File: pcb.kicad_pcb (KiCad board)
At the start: 2 copper layers, 76 parts, among them SW1 SW_Push, U1 ATmega32U4-AU, Y1 16MHz

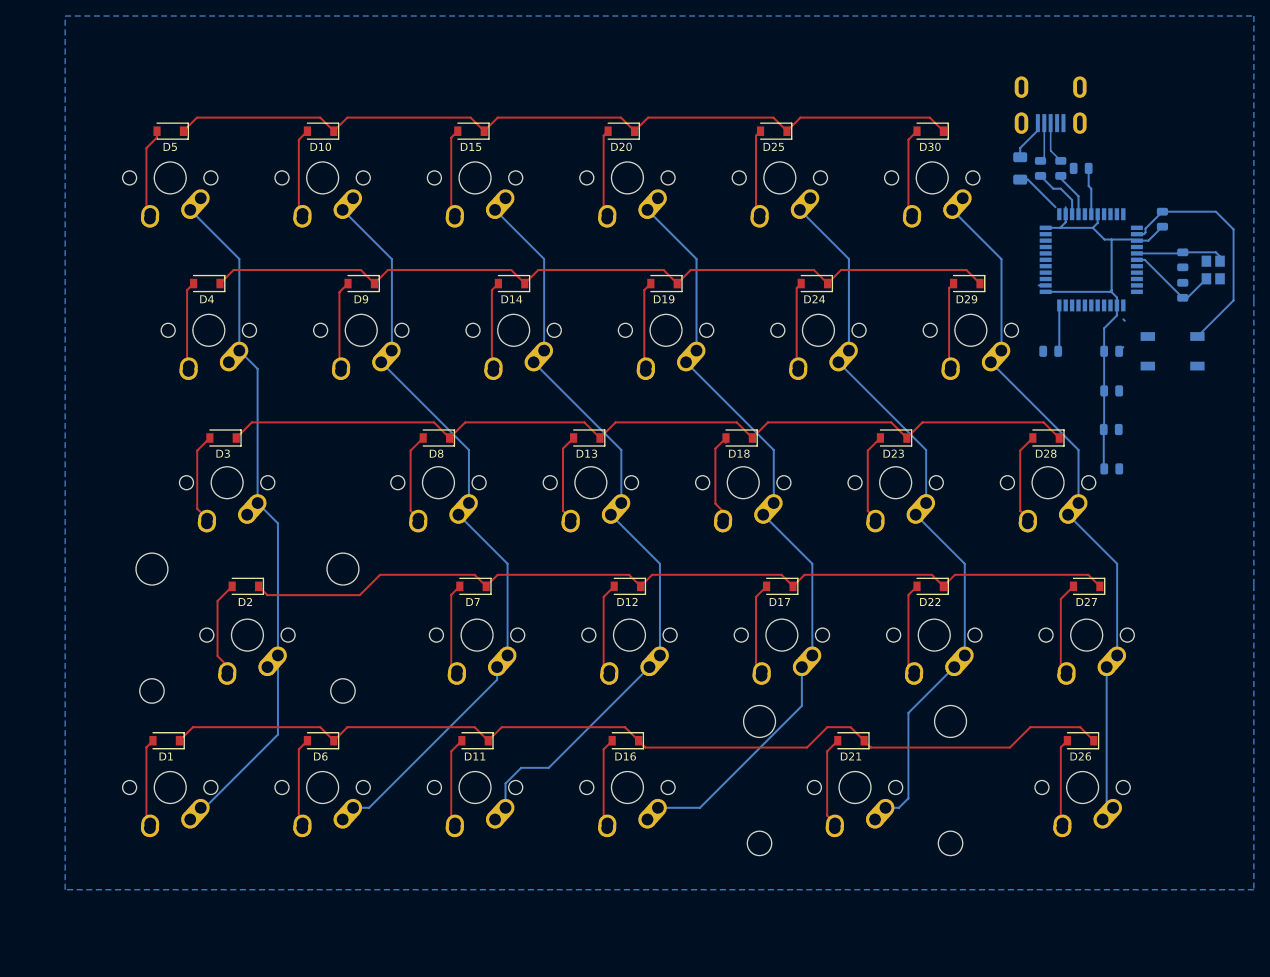
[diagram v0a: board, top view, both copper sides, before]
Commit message: Cleaned PCB
Added hotswap, started new trace routes
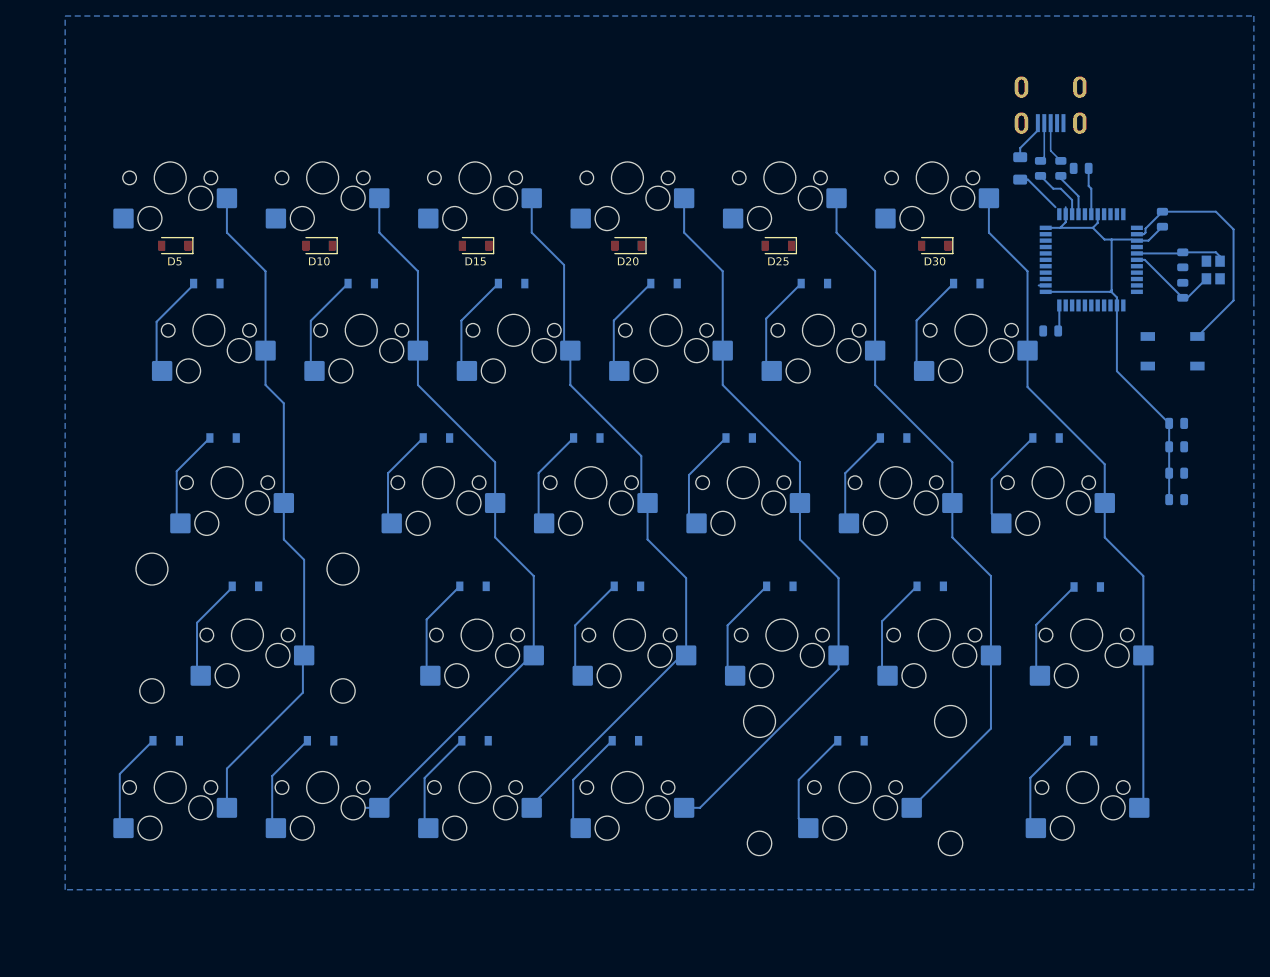
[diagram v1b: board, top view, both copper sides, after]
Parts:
- D1, D11, D12, D13, D14, D16, D17, D18, D19, D2, D21, D22, D23, D24, D26, D27, D28, D29, D3, D4, D6, D7, D8, D9: moved to B.Cu
- MX1, MX10, MX11, MX12, MX13, MX14, MX15, MX16, MX17, MX18, MX19, MX20, MX22, MX23, MX24, MX25, MX26, MX27, MX28, MX29, MX30, MX5, MX6, MX7, MX8, MX9: footprint MX_Alps_Hybrid_Included:MX-1U-NoLED -> MXHotswaps:MX-Hotswap-1U
- MX2, MX21: footprint MX_Alps_Hybrid_Included:MX-2U-NoLED -> MXHotswaps:MX-Hotswap-2U
- MX3: footprint MX_Alps_Hybrid_Included:MX-1.75U-NoLED -> MXHotswaps:MX-Hotswap-1.75U
- MX4: footprint MX_Alps_Hybrid_Included:MX-1.5U-NoLED -> MXHotswaps:MX-Hotswap-1.5U
- moved D20 14.3 mm to (88.1, 108.7)
- moved D15 14.3 mm to (69.1, 108.7)
- moved D25 14.3 mm to (106.9, 108.7)
- moved D30 14.3 mm to (126.5, 108.7)
- moved D5 14.3 mm to (31.5, 108.7)
- moved D10 14.3 mm to (49.5, 108.7)
- moved C7 12.1 mm to (156.7, 130.9)
- moved C3 10.7 mm to (156.7, 133.9)
- moved C2 9.83 mm to (156.7, 137.2)
- moved C1 8.98 mm to (156.7, 140.5)
- moved R4 2.54 mm to (141.0, 119.4)
- moved D27 0.11 mm to (145.5, 151.4)
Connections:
- U1 pad 1: Net-(U1-Pad1) -> unconnected-(U1-Pad1)
- U1 pad 10: Net-(U1-Pad10) -> ROW2
- U1 pad 11: Net-(U1-Pad11) -> ROW3
- U1 pad 12: Net-(U1-Pad12) -> COL2
- U1 pad 18: Net-(U1-Pad18) -> COL5
- U1 pad 19: Net-(U1-Pad19) -> unconnected-(U1-Pad19)
- U1 pad 20: Net-(U1-Pad20) -> unconnected-(U1-Pad20)
- U1 pad 21: Net-(U1-Pad21) -> unconnected-(U1-Pad21)
- U1 pad 22: Net-(U1-Pad22) -> unconnected-(U1-Pad22)
- U1 pad 25: Net-(U1-Pad25) -> unconnected-(U1-Pad25)
- U1 pad 26: Net-(U1-Pad26) -> unconnected-(U1-Pad26)
- U1 pad 27: Net-(U1-Pad27) -> unconnected-(U1-Pad27)
- U1 pad 28: Net-(U1-Pad28) -> ROW4
- U1 pad 29: Net-(U1-Pad29) -> COL0
- U1 pad 30: Net-(U1-Pad30) -> COL1
- U1 pad 31: Net-(U1-Pad31) -> COL3
- U1 pad 32: Net-(U1-Pad32) -> COL4
- U1 pad 36: Net-(U1-Pad36) -> unconnected-(U1-Pad36)
- U1 pad 37: Net-(U1-Pad37) -> unconnected-(U1-Pad37)
- U1 pad 38: Net-(U1-Pad38) -> unconnected-(U1-Pad38)
- U1 pad 39: Net-(U1-Pad39) -> unconnected-(U1-Pad39)
- U1 pad 40: Net-(U1-Pad40) -> unconnected-(U1-Pad40)
- U1 pad 41: Net-(U1-Pad41) -> unconnected-(U1-Pad41)
- U1 pad 42: Net-(U1-Pad42) -> unconnected-(U1-Pad42)
- U1 pad 8: Net-(U1-Pad8) -> ROW0
- U1 pad 9: Net-(U1-Pad9) -> ROW1
- USB1 pad 2: Net-(USB1-Pad2) -> unconnected-(USB1-Pad2)
- USB1 pad 6: Net-(USB1-Pad6) -> unconnected-(USB1-Pad6)
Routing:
- net ROW4: track 122.7 -> 0.00 mm
- net ROW3: track 112.0 -> 0.00 mm
- net ROW2: track 110.9 -> 0.00 mm
- net ROW0: track 102.0 -> 0.00 mm
- net ROW1: track 102.0 -> 0.00 mm
- net Net-(D5-Pad2): track 10.3 -> 0.00 mm
- net Net-(D30-Pad2): track 10.2 -> 0.00 mm
- net Net-(D10-Pad2): track 10.2 -> 0.00 mm
- net Net-(D15-Pad2): track 10.1 -> 0.00 mm
- net Net-(D25-Pad2): track 9.97 -> 0.00 mm
- net Net-(D20-Pad2): track 9.97 -> 0.00 mm
- net +5V: track 63.9 -> 69.8 mm
- net COL1: track 88.6 -> 94.4 mm
- net COL5: track 80.3 -> 85.6 mm
- net COL4: track 84.5 -> 88.3 mm
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
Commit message: V0.2
Replaced Footprint. Trace Routes (almost) done
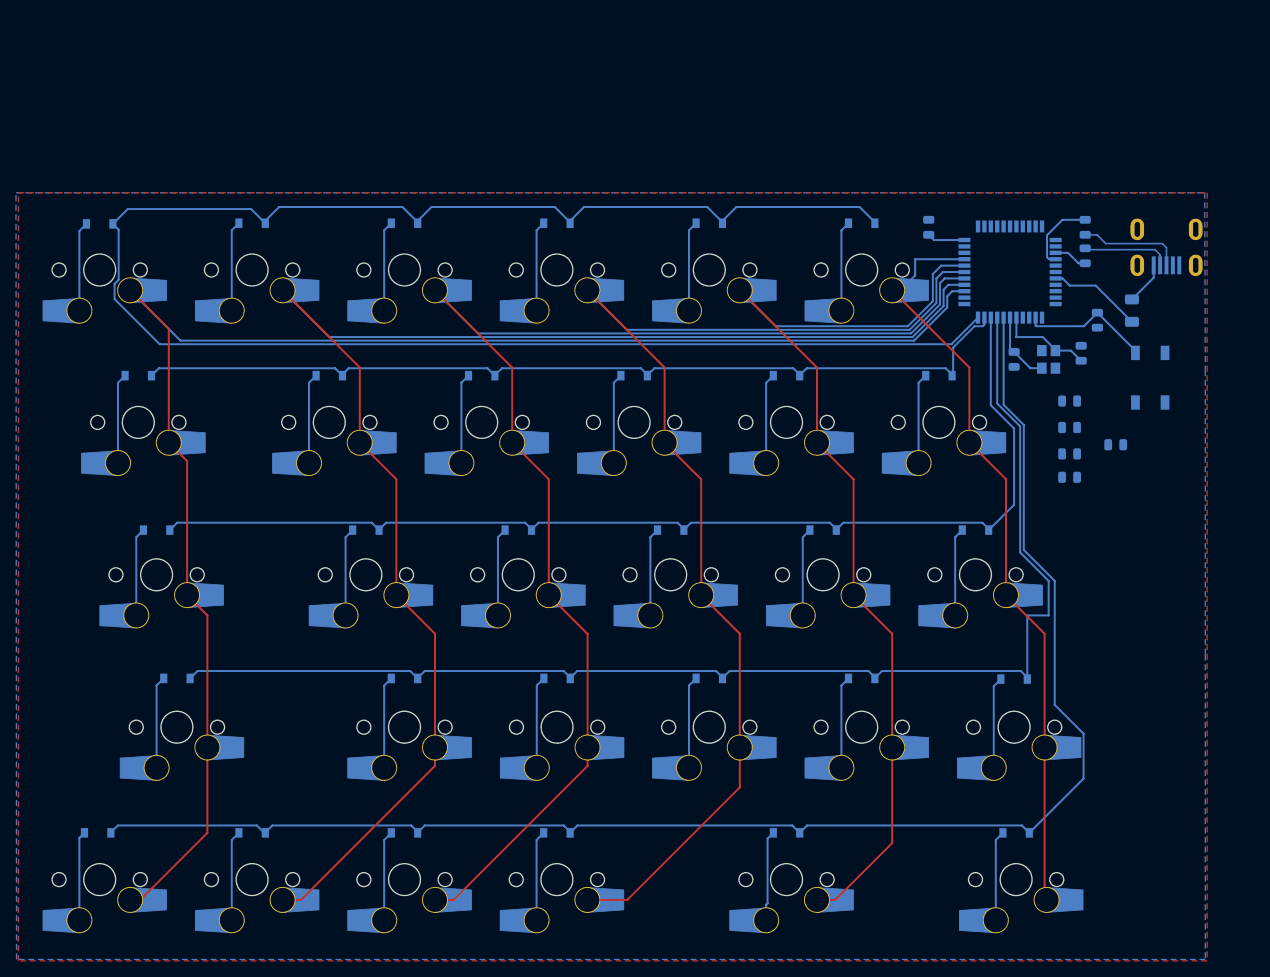
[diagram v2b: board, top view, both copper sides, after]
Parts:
- D10, D15, D20, D25, D30, D5: moved to B.Cu
- MX1, MX10, MX11, MX12, MX13, MX14, MX15, MX16, MX17, MX18, MX19, MX20, MX22, MX23, MX24, MX25, MX26, MX27, MX28, MX29, MX30, MX5, MX6, MX7, MX8, MX9: footprint MXHotswaps:MX-Hotswap-1U -> MXHotswaps:MXOnly-1U-Hotswap-Modified
- MX2, MX21: footprint MXHotswaps:MX-Hotswap-2U -> MXHotswaps:MXOnly-1U-Hotswap-Modified
- MX3: footprint MXHotswaps:MX-Hotswap-1.75U -> MXHotswaps:MXOnly-1U-Hotswap-Modified
- MX4: footprint MXHotswaps:MX-Hotswap-1.5U -> MXHotswaps:MXOnly-1U-Hotswap-Modified
- moved C6 34.8 mm to (149.1, 133.6), turned to 0 degrees
- moved Y1 23.4 mm to (140.7, 122.9)
- moved USB1 22.9 mm to (155.4, 106.7)
- moved C4 22.8 mm to (136.4, 122.9), turned to -90 degrees
- moved F1 22.6 mm to (151.1, 116.8)
- moved R4 20.0 mm to (125.7, 106.4), turned to -90 degrees
- moved C1 18.2 mm to (143.3, 128.1), turned to 180 degrees
- moved C5 17.3 mm to (144.8, 122.2), turned to 90 degrees
- moved R3 15.0 mm to (146.8, 118.0)
- moved C7 15.0 mm to (143.3, 137.7), turned to 180 degrees
- moved D27 14.7 mm to (136.4, 162.9)
- moved MX13 14.7 mm to (74.4, 149.9)
- moved MX17 14.7 mm to (98.3, 168.9)
- moved MX18 14.7 mm to (93.5, 149.9)
- moved MX22 14.7 mm to (117.3, 168.9)
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- renumbered U1 to 32U4
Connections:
- 32U4 pad 10: ROW2 -> unconnected-(32U4-Pad10)
- 32U4 pad 11: ROW3 -> unconnected-(32U4-Pad11)
- 32U4 pad 12: COL2 -> unconnected-(32U4-Pad12)
- 32U4 pad 18: COL5 -> ROW4
- 32U4 pad 19: unconnected-(U1-Pad19) -> ROW3
- 32U4 pad 20: unconnected-(U1-Pad20) -> ROW2
- 32U4 pad 21: unconnected-(U1-Pad21) -> ROW1
- 32U4 pad 22: unconnected-(U1-Pad22) -> ROW0
- 32U4 pad 25: unconnected-(U1-Pad25) -> COL0
- 32U4 pad 26: unconnected-(U1-Pad26) -> COL1
- 32U4 pad 27: unconnected-(U1-Pad27) -> COL2
- 32U4 pad 28: ROW4 -> COL3
- 32U4 pad 29: COL0 -> COL4
- 32U4 pad 30: COL1 -> COL5
- 32U4 pad 31: COL3 -> unconnected-(32U4-Pad31)
- 32U4 pad 32: COL4 -> unconnected-(32U4-Pad32)
- 32U4 pad 8: ROW0 -> unconnected-(32U4-Pad8)
- 32U4 pad 9: ROW1 -> unconnected-(32U4-Pad9)
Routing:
- net ROW0: track 0.00 -> 224.3 mm
- net ROW4: track 0.00 -> 190.3 mm
- net ROW3: track 0.00 -> 159.7 mm
- net ROW2: track 0.00 -> 136.0 mm
- net ROW1: track 0.00 -> 114.1 mm
- net COL0: track 84.7 -> 195.4 mm
- net COL1: track 94.4 -> 184.9 mm
- net COL2: track 92.5 -> 168.0 mm
- net +5V: track 69.8 -> 11.8 mm
- net COL3: track 93.4 -> 148.9 mm
- net COL4: track 88.3 -> 124.4 mm
- net Net-(R3-Pad2): track 29.7 -> 16.5 mm
- net Net-(D25-Pad2): track 0.00 -> 11.3 mm
- net Net-(D20-Pad2): track 0.00 -> 11.3 mm
- net Net-(D15-Pad2): track 0.00 -> 11.3 mm
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- added copper zone on F.Cu, net +5V

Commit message: ...
...
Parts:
- moved C7 36.6 mm to (131.2, 103.1), turned to 90 degrees
- moved C3 32.9 mm to (134.1, 103.1), turned to 90 degrees
- moved C2 28.9 mm to (137.4, 103.1), turned to 90 degrees
- moved C1 25.2 mm to (140.7, 103.1), turned to 90 degrees
- moved C6 21.3 mm to (148.3, 112.3)
- moved SW1 4.02 mm to (150.1, 127.5)
- moved R3 0.18 mm to (146.8, 117.9), turned to -90 degrees
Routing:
- net ROW0: track 224.3 -> 250.7 mm
- net +5V: track 11.8 -> 28.0 mm
- net GND: track 0.00 -> 9.63 mm
- net Net-(C6-Pad1): track 0.00 -> 5.91 mm
- net Net-(R3-Pad2): track 16.5 -> 15.1 mm
- net COL5: track 94.7 -> 93.5 mm
- net ROW4: track 190.3 -> 191.0 mm
- removed copper zone on F.Cu, net +5V
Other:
- board outline added: 148.3 x 97.3 mm

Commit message: Spaghetti Junction
Yummm
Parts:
- added C8: 0.1uF, Capacitor_SMD:C_0805_2012Metric, F.Cu at (139.2, 114.8)
- added C9: 0.1uF, Capacitor_SMD:C_0805_2012Metric, F.Cu at (138.4, 111.5)
- C1, C2, C3, C7: moved to F.Cu
- moved C7 13.3 mm to (135.9, 115.6), turned to 180 degrees
- moved C3 9.27 mm to (132.6, 112.3)
- moved C1 9.04 mm to (133.6, 108.7), turned to 0 degrees
- moved C2 5.61 mm to (137.9, 108.7), turned to 180 degrees
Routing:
- net +5V: track 28.0 -> 49.0 mm, vias 0 -> 6
- net GND: track 9.63 -> 21.8 mm, vias 0 -> 1
